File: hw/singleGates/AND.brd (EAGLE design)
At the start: 8 parts, among them Q1 BC817, Q2 BC817, Q3 BC817

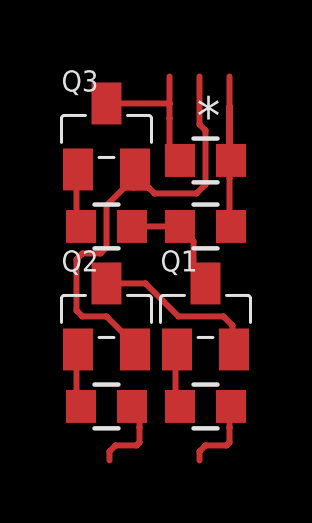
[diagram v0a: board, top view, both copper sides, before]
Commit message: Trying to mimize gates some more
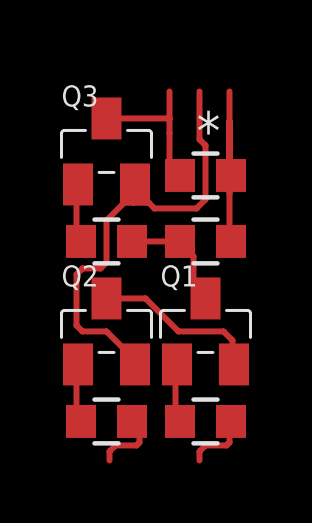
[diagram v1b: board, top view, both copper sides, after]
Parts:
- moved Q1 0.50 mm to (5.20, 4.40)
- moved Q2 0.50 mm to (1.90, 4.40)
- moved Q3 0.50 mm to (1.90, 10.4)
- moved R1 0.50 mm to (5.20, 1.40)
- moved R2 0.50 mm to (1.90, 1.40)
- moved R3 0.50 mm to (5.20, 7.40)
- moved R4 0.50 mm to (1.90, 7.40)
- moved R5 0.50 mm to (5.20, 9.60)
